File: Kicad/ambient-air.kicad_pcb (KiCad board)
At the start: 2 copper layers, 65.1 x 35 mm, 49 parts, among them J1 USB_C_Receptacle_USB2.0_14P, J2 Conn_01x02, J3 Conn_01x04, J4 Conn_01x04, SW1 SW_Push, SW2 MINI MSK12CO2, SW3 SW_Push, U1 MCP73831T-2ACI/MC, U10 BQ27441-G1, U11 TPS2116DRL, U2 AP7361C-33SP-13, U3 ESP32-C3-WROOM-02, U4 TPD4E05U06DQA, U5 SHT4x, U6 STCC4-D1, U7 AHT20_C2757850, U8 SGP40-D-R4, U9 ICP-20100

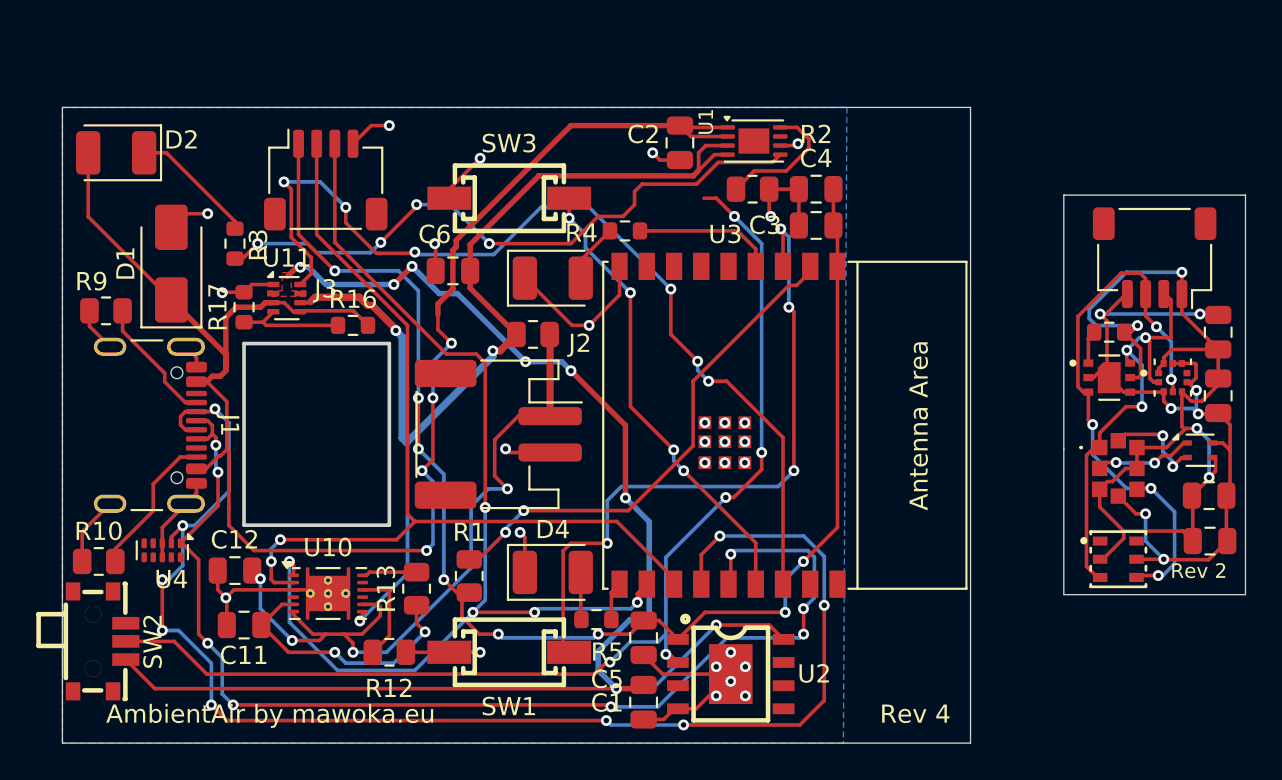
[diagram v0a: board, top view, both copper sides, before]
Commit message: Add RTC to pcb and move sgp40 from sensor to main pcb
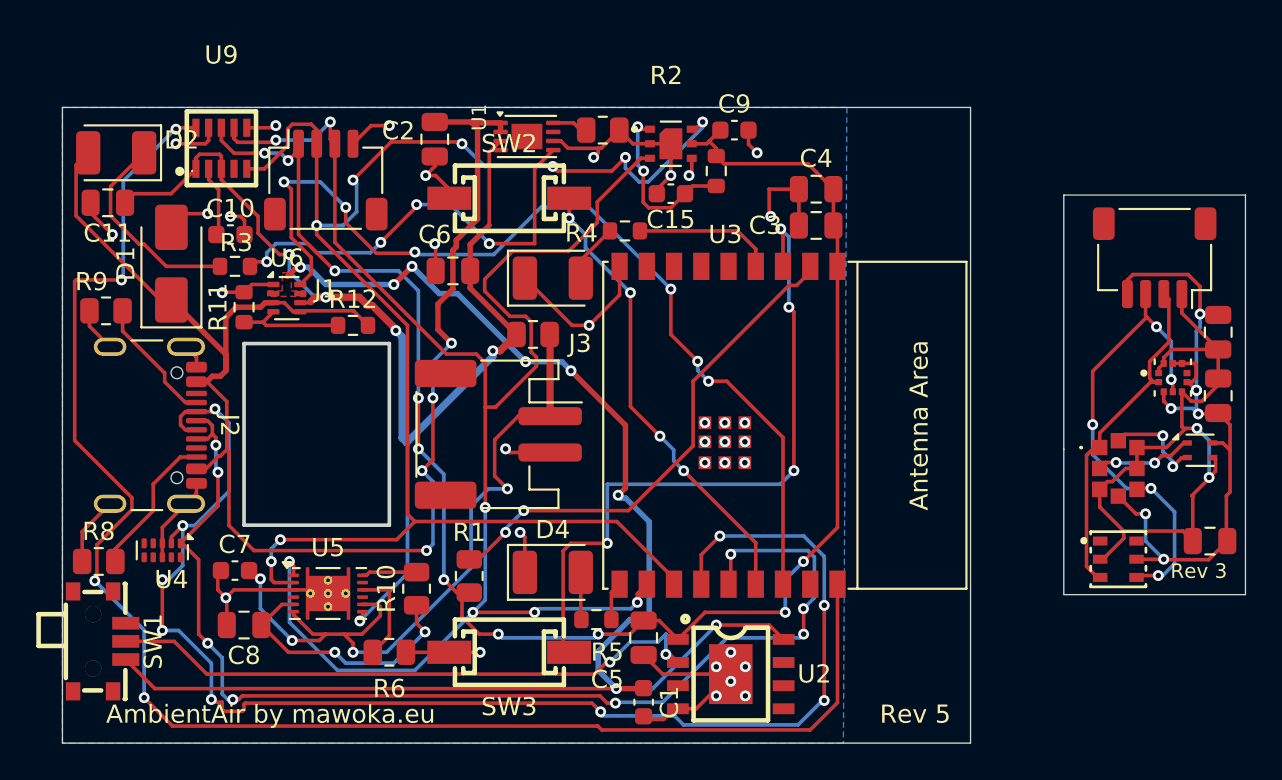
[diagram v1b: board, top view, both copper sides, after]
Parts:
- added C10: 1µF, Capacitor_SMD:C_0603_1608Metric, F.Cu at (39.2, 37.0)
- added C11: 100nF, Capacitor_SMD:C_0805_2012Metric, F.Cu at (32.5, 35.2)
- added C15: 1µF, Capacitor_SMD:C_0603_1608Metric, F.Cu at (63.5, 34.8)
- added U9: RX8111CE, easyeda2kicad:OSC-SMD_10P-L3.2-W2.5-BL-1, F.Cu at (38.8, 32.2)
- C1, C9: footprint Capacitor_SMD:C_0805_2012Metric -> Capacitor_SMD:C_0603_1608Metric
- C7: renamed from C12; footprint Capacitor_SMD:C_0805_2012Metric -> Capacitor_SMD:C_0603_1608Metric
- moved C9 33.0 mm to (67.0, 31.2)
- moved U7 27.4 mm to (63.5, 32.0)
- moved R13 23.4 mm to (66.0, 33.5), turned to 90 degrees
- moved C2 13.5 mm to (50.5, 31.8)
- moved U1 12.5 mm to (55.6, 31.6)
- moved R2 8.87 mm to (59.8, 31.2)
- moved R3 1.25 mm to (39.5, 38.8), turned to 0 degrees
- renumbered C10 to C12, C8 to C13, C7 to C14, C11 to C8, J3 to J1, J1 to J2, J2 to J3, R13 to R10, R17 to R11, R16 to R12, R6 to R13, R12 to R6, R11 to R7, R10 to R8, SW2 to SW1, SW3 to SW2, SW1 to SW3, U9 to U10, U7 to U11, U6 to U12, U10 to U5, U11 to U6, U8 to U7, U5 to U8
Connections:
- C9 pad 1: +3V3_EXT -> +3V3
- C9 pad 2: GND_EXT -> GND
- R13 pad 2: +3V3_EXT -> +3V3
- U3 pad 18: unconnected-(U3-GPIO0/ADC1_CH0/XTAL_32K_P-Pad18) -> /TIME_INT
- U7 pad 2: GND_EXT -> GND
- U7 pad 3: /SDA_EXT -> /SDA
- U7 pad 4: GND_EXT -> GND
- U7 pad 5: +3V3_EXT -> +3V3
- U7 pad 6: /SCL_EXT -> /SCL
- U7 pad 7: GND_EXT -> GND
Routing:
- net /TIME_INT: track 0.00 -> 85.6 mm, vias 0 -> 4
- net /SCL: track 50.4 -> 85.4 mm, vias 2 -> 8
- net /SDA: track 57.7 -> 88.2 mm, vias 5 -> 7
- net /EN_VBAT: track 61.5 -> 33.4 mm, vias 5 -> 2
- net GND: track 70.1 -> 89.5 mm, vias 28 -> 34
- net +3V3: track 76.9 -> 92.9 mm, vias 8 -> 10
- net +3V3_EXT: track 54.1 -> 39.5 mm, vias 4 -> 2
- net Net-(U1-STAT): track 35.2 -> 24.3 mm
- net VBUS: track 90.0 -> 81.7 mm
- net Net-(U7-VDD): track 1.83 -> 9.68 mm, vias 0 -> 2
- net /SCL_EXT: track 24.3 -> 18.9 mm, vias 3 -> 0
- net Net-(U1-PROG): track 7.29 -> 2.10 mm
- net /VBAT: track 58.2 -> 63.2 mm, vias 3 -> 5
- net /SDA_EXT: track 31.7 -> 26.7 mm
- net Net-(D2-K): track 6.96 -> 11.4 mm
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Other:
- board text added: "Rev 3"
- board text added: "Rev 5"
- board text removed: "Rev 2"
- board text removed: "Rev 4"
